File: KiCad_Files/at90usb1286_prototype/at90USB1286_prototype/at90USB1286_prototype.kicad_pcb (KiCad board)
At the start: 2 copper layers, 45 parts, among them J1 USB_C_Receptacle_USB2.0, J2 Conn_01x09, J3 Conn_01x03, K1 KEYSW, K2 KEYSW, K3 KEYSW, K4 KEYSW, SW1 SW_Push, U1 AT90USB1286-AU, U2 IS31FL3731-QF, Y1 Crystal_GND24

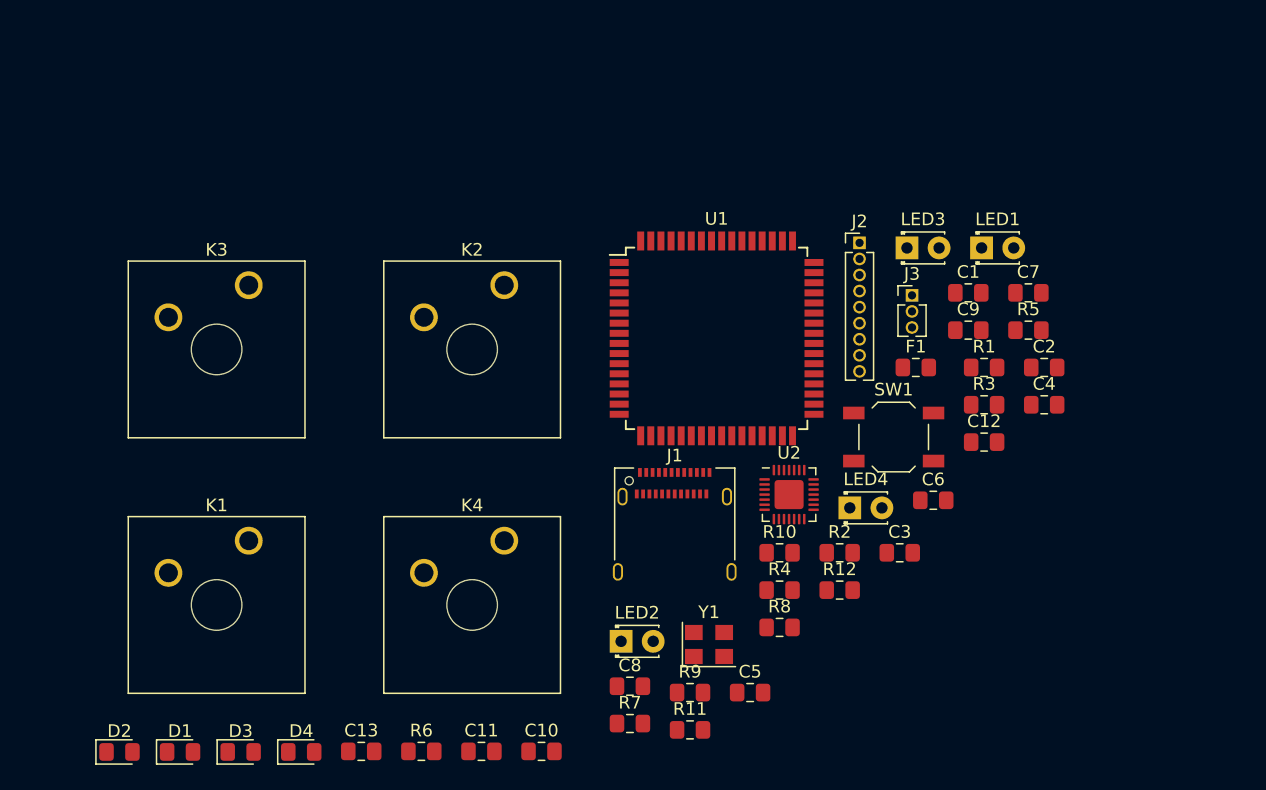
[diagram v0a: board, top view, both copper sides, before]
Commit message: Changed matrix I2C, and finished PCB
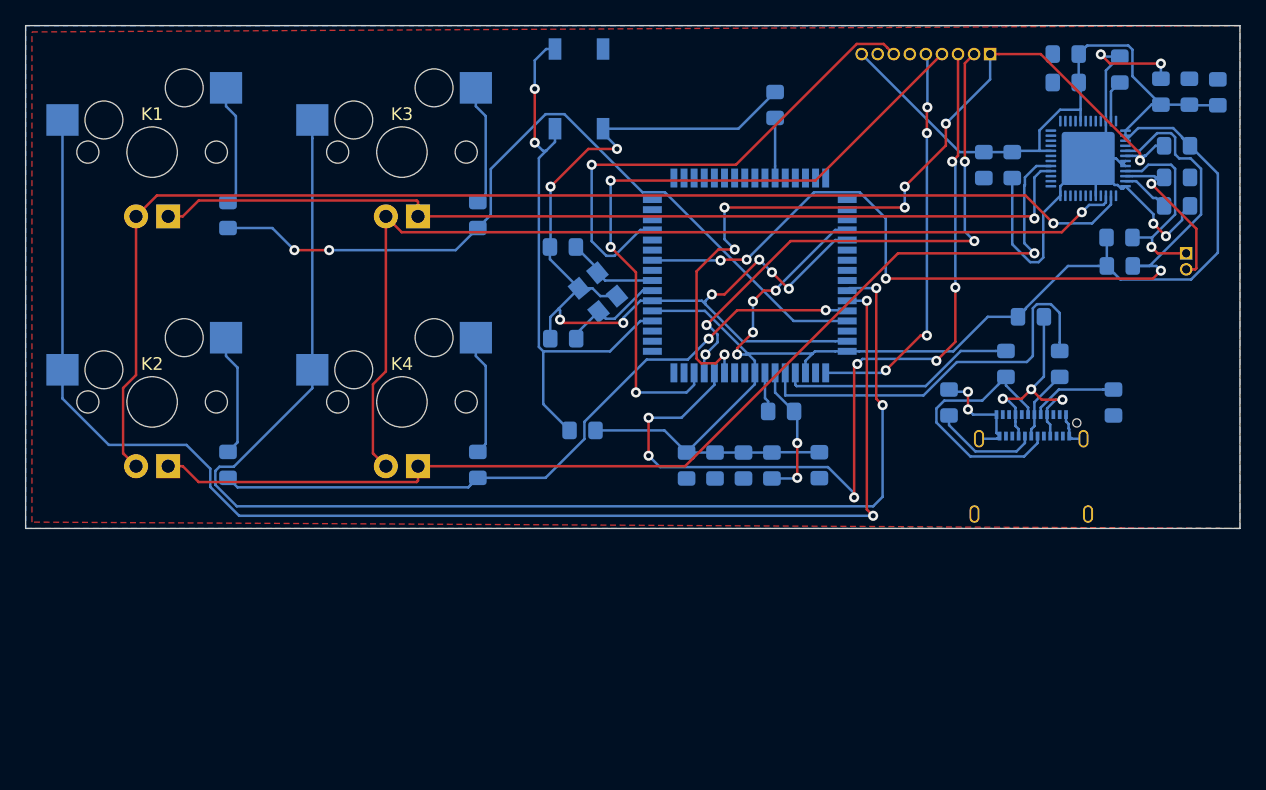
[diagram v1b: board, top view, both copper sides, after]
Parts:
- added C14: 4.7u, Capacitor_SMD:C_0805_2012Metric_Pad1.15x1.40mm_HandSolder, B.Cu at (178.5, 79.7)
- added C15: 4.7u, Capacitor_SMD:C_0805_2012Metric_Pad1.15x1.40mm_HandSolder, B.Cu at (180.8, 79.8)
- C1, C13, C2, C3, C4, C5, C6, C7, C8, D1, D2, D3, D4, F1, J1, J2, R1, R10, R11, R12, R2, R3, R4, R5, R6, R7, R8, R9, SW1, U1, Y1: moved to B.Cu
- C10: value 0.1u -> 4.7u; moved to B.Cu
- C11: value 10u -> 0.1u; moved to B.Cu
- C12: value 10u -> 4.7u; moved to B.Cu
- C9: value 0.22u -> 0.1u; moved to B.Cu
- J3: value Conn_01x03 -> Conn_01x02; footprint Connector_PinHeader_1.27mm:PinHeader_1x03_P1.27mm_Vertical -> Connector_PinHeader_1.27mm:PinHeader_1x02_P1.27mm_Vertical; moved to B.Cu
- K1, K2, K3, K4: footprint Button_Switch_Keyboard:SW_Cherry_MX_1.00u_Plate -> MX_Only:MXOnly-1U-Hotswap
- LED1: value C1-1 -> 1A; footprint LED_THT:LED_D1.8mm_W3.3mm_H2.4mm -> MX_Only:MXOnly-LEDONLY
- LED2: value C1-2 -> 2A; footprint LED_THT:LED_D1.8mm_W3.3mm_H2.4mm -> MX_Only:MXOnly-LEDONLY
- LED3: value C2-1 -> 1B; footprint LED_THT:LED_D1.8mm_W3.3mm_H2.4mm -> MX_Only:MXOnly-LEDONLY
- LED4: value C2-2 -> 2B; footprint LED_THT:LED_D1.8mm_W3.3mm_H2.4mm -> MX_Only:MXOnly-LEDONLY
- U2: value IS31FL3731-QF -> IS31FL3733-QF; footprint Package_DFN_QFN:QFN-28-1EP_4x4mm_P0.4mm_EP2.3x2.3mm -> Package_DFN_QFN:QFN-48-1EP_6x6mm_P0.4mm_EP4.2x4.2mm; moved to B.Cu
- moved C13 81.9 mm to (176.2, 79.7), turned to 270 degrees
- moved C11 70.2 mm to (168.7, 79.0)
- moved LED1 66.0 mm to (96.5, 84.5)
- moved R6 58.3 mm to (145.8, 80.8), turned to 90 degrees
- moved C10 58.1 mm to (162.2, 85.5), turned to 90 degrees
- moved R11 56.6 mm to (177.5, 88.8)
- moved R7 53.0 mm to (173.0, 93.5)
- moved R9 49.5 mm to (173.0, 91.2)
- moved R8 49.4 mm to (177.5, 84.0), turned to 180 degrees
- moved R12 46.7 mm to (173.0, 78.0), turned to 90 degrees
- moved D3 46.4 mm to (122.2, 89.5), turned to 90 degrees
- moved R10 43.2 mm to (177.5, 86.5)
- moved D1 42.6 mm to (102.5, 89.5), turned to 90 degrees
- moved LED2 41.6 mm to (96.5, 104.2)
- moved LED3 40.6 mm to (116.2, 84.5)
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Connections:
- C10 pad 1: Net-(C10-Pad1) -> GND
- C10 pad 2: GND -> VCC
- C9 pad 1: Net-(C9-Pad1) -> GND
- C9 pad 2: /IN -> VCC
- J3 pad 1: /IN -> /INTB
- J3 pad 2: /INTB -> /SDB
- LED1 pad 1: /CA1 -> /SW1
- LED1 pad 2: /CA2 -> /CS1
- LED2 pad 1: /CA1 -> /SW1
- LED2 pad 2: Net-(LED2-Pad2) -> /CS2
- LED3 pad 1: /CA2 -> /SW2
- LED3 pad 2: /CA1 -> /CS1
- LED4 pad 1: /CA2 -> /SW2
- LED4 pad 2: Net-(LED2-Pad2) -> /CS2
- R10 pad 2: VCC -> GND
- U2 pad 12: Net-(U2-Pad12) -> GND
- U2 pad 16: Net-(C10-Pad1) -> /CS1
- U2 pad 17: Net-(C9-Pad1) -> /CS2
- U2 pad 18: Net-(R11-Pad1) -> Net-(U2-Pad18)
- U2 pad 19: /SDA -> Net-(U2-Pad19)
- U2 pad 2: VCC -> /SW1
- U2 pad 20: /SCK -> VCC
- U2 pad 21: /CA1 -> Net-(U2-Pad21)
- U2 pad 22: /CA2 -> Net-(U2-Pad22)
- U2 pad 29: GND -> VCC
- U2 pad 3: /SDB -> /SW2
- U2 pad 4: /INTB -> Net-(U2-Pad4)
- U2 pad 6: Net-(R12-Pad1) -> Net-(U2-Pad6)
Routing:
- net VCC: track 0.00 -> 162.0 mm, vias 0 -> 4
- net GND: track 0.00 -> 158.8 mm, vias 0 -> 16
- net /COL0: track 0.00 -> 109.5 mm, vias 0 -> 2
- net /COL1: track 0.00 -> 105.5 mm, vias 0 -> 2
- net /SW1: track 0.00 -> 100.6 mm, vias 0 -> 1
- net /CS2: track 0.00 -> 85.9 mm, vias 0 -> 1
- net /SW2: track 0.00 -> 79.5 mm, vias 0 -> 1
- net /CS1: track 0.00 -> 75.0 mm, vias 0 -> 1
- net /MOSI: track 0.00 -> 70.3 mm, vias 0 -> 7
- net /SDA: track 0.00 -> 69.9 mm, vias 0 -> 4
- net /SCK: track 0.00 -> 67.2 mm, vias 0 -> 7
- net /ROW0: track 0.00 -> 63.0 mm, vias 0 -> 2
- net /ROW1: track 0.00 -> 55.9 mm, vias 0 -> 2
- net /CS: track 0.00 -> 53.7 mm, vias 0 -> 3
- net Net-(R5-Pad1): track 0.00 -> 44.6 mm, vias 0 -> 2
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- added copper zone on B.Cu, net GND
- added copper zone on F.Cu, net GND
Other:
- board outline added: 96 x 39.8 mm
- net class Default: trace_width 0.25 -> 0.2
